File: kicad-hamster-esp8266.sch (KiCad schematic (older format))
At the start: 35 parts, among them J1 Power Supply, J2 UART, J3 Screw_Terminal_01x02, J4 Screw_Terminal_01x02, J5 Screw_Terminal_01x02, J6 Screw_Terminal_01x02, Q1 IRLML5203, SW1 Reset, SW2 Flash, U1 ADM706P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

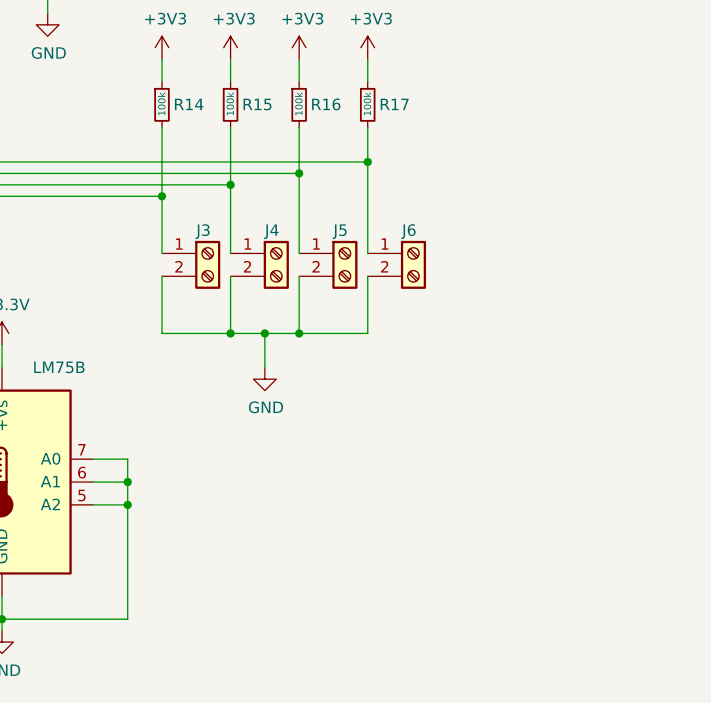
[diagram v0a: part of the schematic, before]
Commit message: pcb: text and updated footprint
- modify footprint of reed switch connector
- add silkscreen text

Signed-off-by: Sergey Matyukevich <geomatsi@gmail.com>
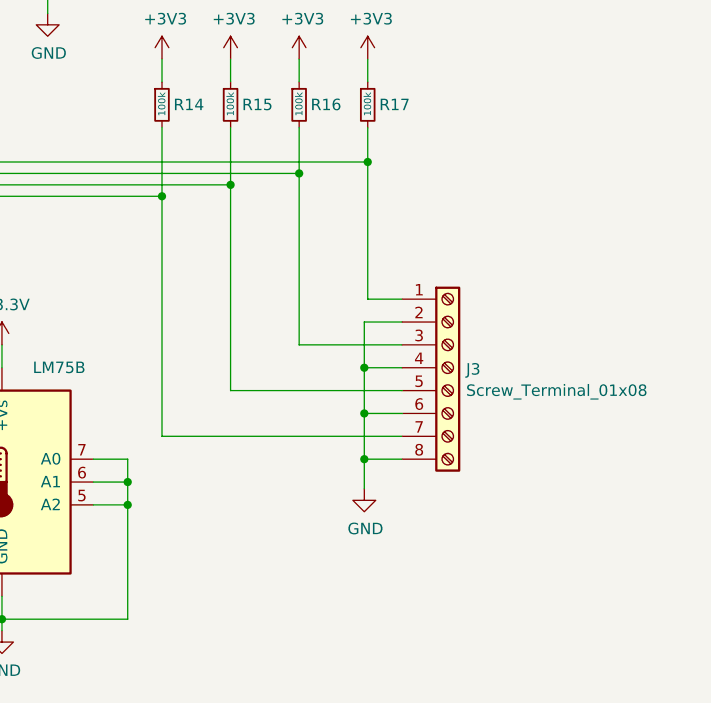
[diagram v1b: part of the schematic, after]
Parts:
- removed J3, J4, J5, J6: Screw_Terminal_01x02, TerminalBlock_Phoenix:TerminalBlock_Phoenix_PT-1,5-2-3.5-H_1x02_P3.50mm_Horizontal, symbol Connector:Screw_Terminal_01x02
- added J3: Screw_Terminal_01x08, TerminalBlock_Phoenix:TerminalBlock_Phoenix_MKDS-1,5-8_1x08_P5.00mm_Horizontal, symbol Connector:Screw_Terminal_01x08
- J1: footprint TerminalBlock_Phoenix:TerminalBlock_Phoenix_PT-1,5-2-3.5-H_1x02_P3.50mm_Horizontal -> TerminalBlock_Phoenix:TerminalBlock_Phoenix_MKDS-1,5-2_1x02_P5.00mm_Horizontal
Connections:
- net GND: now also J3.2 (Pin_2), J3.4 (Pin_4), J3.6 (Pin_6), J3.8 (Pin_8)
- net at R14.2, U3.4 (GPIO16): now also J3.7 (Pin_7)
- net at R15.2, U3.5 (GPIO14): now also J3.5 (Pin_5)
- net at R17.2, U3.6 (GPIO12): now also J3.1 (Pin_1)
- net at R16.2, U3.7 (GPIO13): now also J3.3 (Pin_3)
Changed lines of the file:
@@
 F 0 "J1" H 1500 5100 50  0000 C CNN
 F 1 "Power Supply" H 1850 5300 50  0000 C CNN
-F 2 "TerminalBlock_Phoenix:TerminalBlock_Phoenix_PT-1,5-2-3.5-H_1x02_P3.50mm_Horizontal" H 1500 5350 50  0001 C CNN
+F 2 "TerminalBlock_Phoenix:TerminalBlock_Phoenix_MKDS-1,5-2_1x02_P5.00mm_Horizontal" H 1500 5350 50  0001 C CNN
 F 3 "~" H 1500 5350 50  0001 C CNN
 	1    1500 5350
@@
 Wire Wire Line
 	6100 3300 6750 3300
-Connection ~ 8500 3900
 Wire Wire Line
 	8500 3900 8500 3750
-Connection ~ 8200 3950
 Wire Wire Line
 	8200 3950 8200 3750
-Connection ~ 7900 4000
 Wire Wire Line
 	7900 3750 7900 4000
-Connection ~ 7600 4050
 Wire Wire Line
 	7600 4050 7600 3750
@@
 	6700 3950 8200 3950
 Wire Wire Line
-	6750 3900 8500 3900
-Wire Wire Line
-	7600 4650 7900 4650
-Wire Wire Line
-	8050 4650 8200 4650
-Connection ~ 8050 4650
-Wire Wire Line
-	8050 4800 8050 4650
-Connection ~ 8200 4650
-Connection ~ 7900 4650
-Wire Wire Line
-	7900 4650 8050 4650
-Wire Wire Line
 	7900 3450 7900 3550
-Wire Wire Line
-	8200 4650 8500 4650
 $Comp
 L Device:R_Small R15
@@
 L power:GND #PWR0123
 U 1 1 5F136815
-P 8050 4800
-F 0 "#PWR0123" H 8050 4550 50  0001 C CNN
-F 1 "GND" H 8055 4625 50  0000 C CNN
-F 2 "" H 8050 4800 50  0001 C CNN
-F 3 "" H 8050 4800 50  0001 C CNN
-	1    8050 4800
+P 8485 5330
+F 0 "#PWR0123" H 8485 5080 50  0001 C CNN
+F 1 "GND" H 8490 5155 50  0000 C CNN
+F 2 "" H 8485 5330 50  0001 C CNN
+F 3 "" H 8485 5330 50  0001 C CNN
+	1    8485 5330
 	1    0    0    -1
 $EndComp
@@
 Wire Wire Line
 	4550 3100 4550 3200
-$Comp
-L Connector:Screw_Terminal_01x02 J6
-U 1 1 5F1A7DB1
-P 8700 4300
-F 0 "J6" H 8650 4400 50  0000 L CNN
-F 1 "Screw_Terminal_01x02" H 8780 4200 50  0001 L CNN
-F 2 "TerminalBlock_Phoenix:TerminalBlock_Phoenix_PT-1,5-2-3.5-H_1x02_P3.50mm_Horizontal" H 8700 4300 50  0001 C CNN
-F 3 "~" H 8700 4300 50  0001 C CNN
-	1    8700 4300
-	1    0    0    -1
-$EndComp
-$Comp
-L Connector:Screw_Terminal_01x02 J5
-U 1 1 5F1A9503
-P 8400 4300
-F 0 "J5" H 8350 4400 50  0000 L CNN
-F 1 "Screw_Terminal_01x02" H 8480 4200 50  0001 L CNN
-F 2 "TerminalBlock_Phoenix:TerminalBlock_Phoenix_PT-1,5-2-3.5-H_1x02_P3.50mm_Horizontal" H 8400 4300 50  0001 C CNN
-F 3 "~" H 8400 4300 50  0001 C CNN
-	1    8400 4300
-	1    0    0    -1
-$EndComp
-$Comp
-L Connector:Screw_Terminal_01x02 J4
-U 1 1 5F1AE8E4
-P 8100 4300
-F 0 "J4" H 8050 4400 50  0000 L CNN
-F 1 "Screw_Terminal_01x02" H 8180 4200 50  0001 L CNN
-F 2 "TerminalBlock_Phoenix:TerminalBlock_Phoenix_PT-1,5-2-3.5-H_1x02_P3.50mm_Horizontal" H 8100 4300 50  0001 C CNN
-F 3 "~" H 8100 4300 50  0001 C CNN
-	1    8100 4300
-	1    0    0    -1
-$EndComp
-$Comp
-L Connector:Screw_Terminal_01x02 J3
-U 1 1 5F1AF1CC
-P 7800 4300
-F 0 "J3" H 7750 4400 50  0000 L CNN
-F 1 "Screw_Terminal_01x02" H 7880 4200 50  0001 L CNN
-F 2 "TerminalBlock_Phoenix:TerminalBlock_Phoenix_PT-1,5-2-3.5-H_1x02_P3.50mm_Horizontal" H 7800 4300 50  0001 C CNN
-F 3 "~" H 7800 4300 50  0001 C CNN
-	1    7800 4300
-	1    0    0    -1
-$EndComp
-Wire Wire Line
-	7600 4050 7600 4300
-Wire Wire Line
-	7600 4400 7600 4650
-Wire Wire Line
-	7900 4400 7900 4650
-Wire Wire Line
-	7900 4000 7900 4300
-Wire Wire Line
-	8200 4400 8200 4650
-Wire Wire Line
-	8200 3950 8200 4300
-Wire Wire Line
-	8500 4400 8500 4650
-Wire Wire Line
-	8500 3900 8500 4300
 Wire Wire Line
 	6100 3100 6350 3100
@@
 	6400 3200 6400 5000
 Connection ~ 6400 5000
+$Comp
+L Connector:Screw_Terminal_01x08 J3
+U 1 1 5F20B454
+P 8850 4800
+F 0 "J3" H 8930 4793 50  0000 L CNN
+F 1 "Screw_Terminal_01x08" H 8930 4700 50  0000 L CNN
+F 2 "TerminalBlock_Phoenix:TerminalBlock_Phoenix_MKDS-1,5-8_1x08_P5.00mm_Horizontal" H 8850 4800 50  0001 C CNN
+F 3 "~" H 8850 4800 50  0001 C CNN
+	1    8850 4800
+	1    0    0    -1
+$EndComp
+Wire Wire Line
+	6750 3900 8500 3900
+Wire Wire Line
+	8500 3900 8500 4500
+Wire Wire Line
+	8500 4500 8650 4500
+Connection ~ 8500 3900
+Wire Wire Line
+	8650 4700 8200 4700
+Wire Wire Line
+	8200 4700 8200 3950
+Connection ~ 8200 3950
+Wire Wire Line
+	7900 4000 7900 4900
+Wire Wire Line
+	7900 4900 8650 4900
+Connection ~ 7900 4000
+Wire Wire Line
+	7600 4050 7600 5100
+Wire Wire Line
+	7600 5100 8650 5100
+Connection ~ 7600 4050
+Wire Wire Line
+	8485 5330 8485 5200
+Wire Wire Line
+	8485 4600 8650 4600
+Wire Wire Line
+	8650 4800 8485 4800
+Connection ~ 8485 4800
+Wire Wire Line
+	8485 4800 8485 4600
+Wire Wire Line
+	8650 5000 8485 5000
+Connection ~ 8485 5000
+Wire Wire Line
+	8485 5000 8485 4800
+Wire Wire Line
+	8650 5200 8485 5200
+Connection ~ 8485 5200
+Wire Wire Line
+	8485 5200 8485 5000
 $EndSCHEMATC
